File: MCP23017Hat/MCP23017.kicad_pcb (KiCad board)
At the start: 2 copper layers, 65 x 56 mm, 12 parts, among them J0 RPi_GPIO, J1 Address Jumper, T1 GP0, T2 GP1, U1 MCP23017

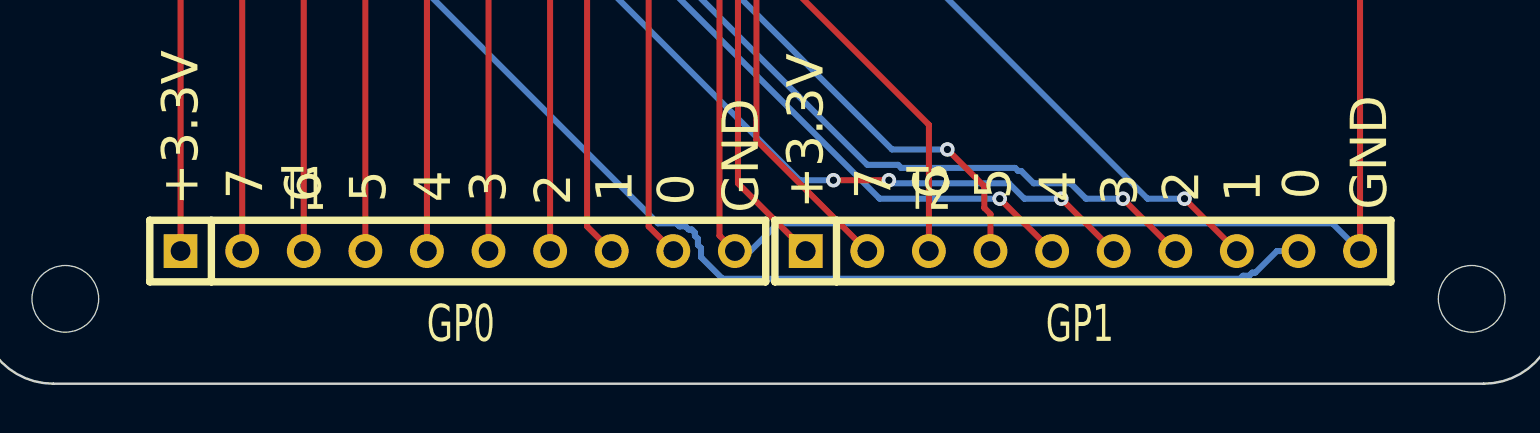
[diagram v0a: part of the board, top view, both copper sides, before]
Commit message: Update screw terminals on all HATs.
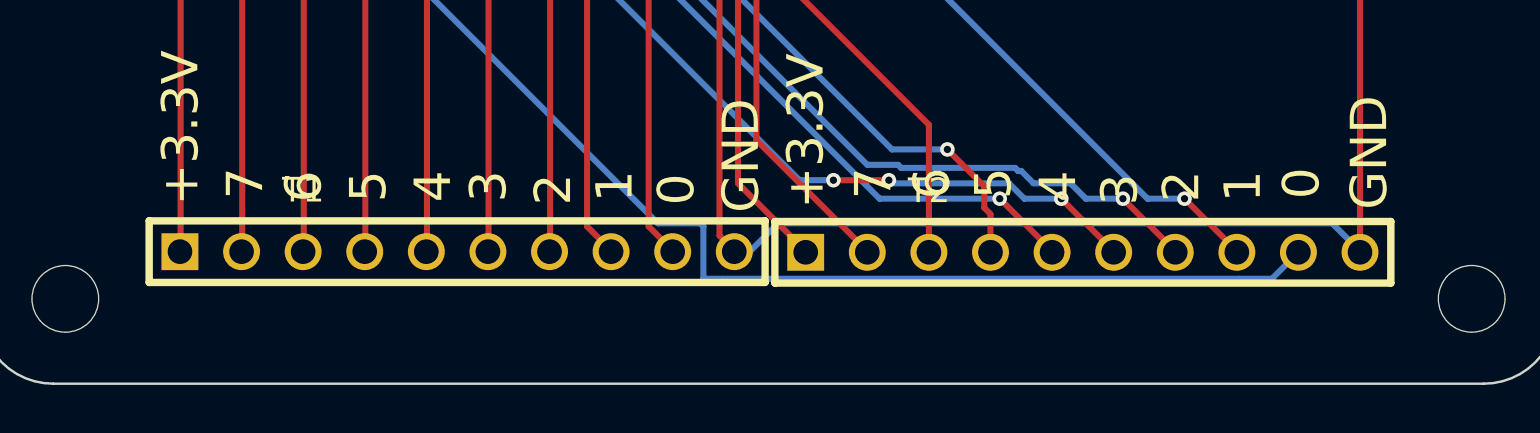
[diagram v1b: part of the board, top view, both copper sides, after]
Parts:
- T1, T2: footprint SIL-10 -> ScrewTerm_2.54-10
- moved T1 6.38 mm to (51.4, 82.4)
- moved T2 6.35 mm to (77.2, 82.5)
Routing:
- net N-000009: track 52.3 -> 53.1 mm

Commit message: Minor updates
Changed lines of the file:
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@@
   )
   (module ScrewTerm_2.54-10 (layer F.Cu)
-    (at 77.216 82.4738)
+    (at 77.216 82.4484)
     (descr "Screw Terminals, 2.54 pitch, 10 position")
     (tags CONN)

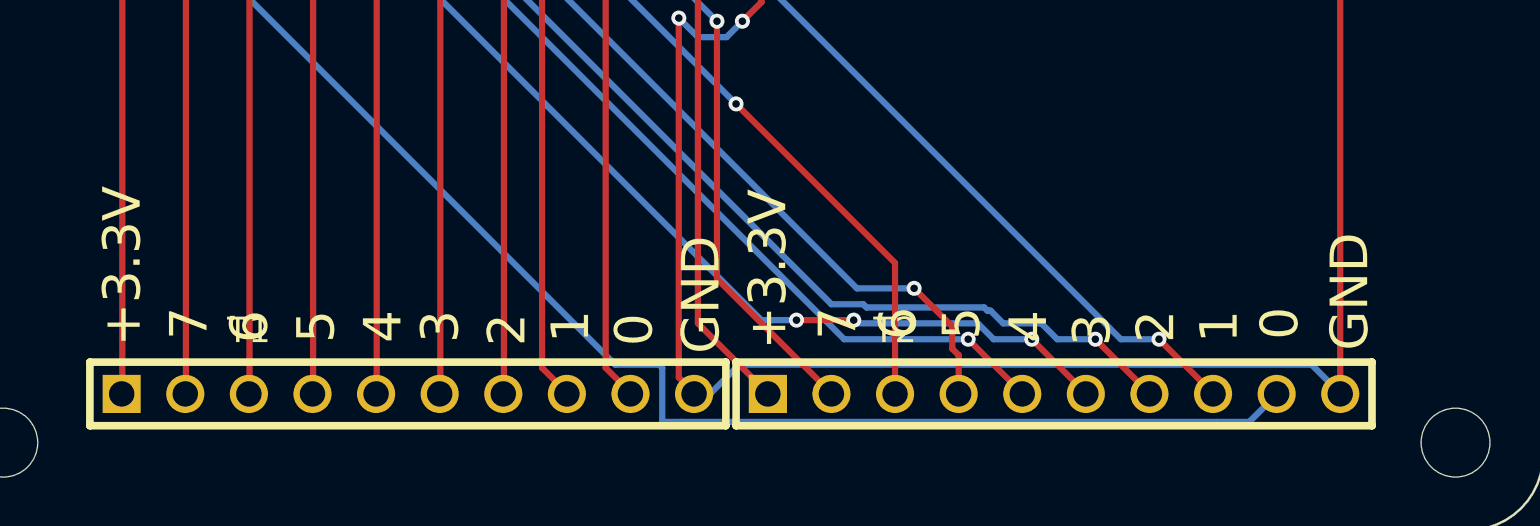
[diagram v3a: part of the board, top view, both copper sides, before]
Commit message: Move terminal markings to be more visible once the terminal blocks have been installed.
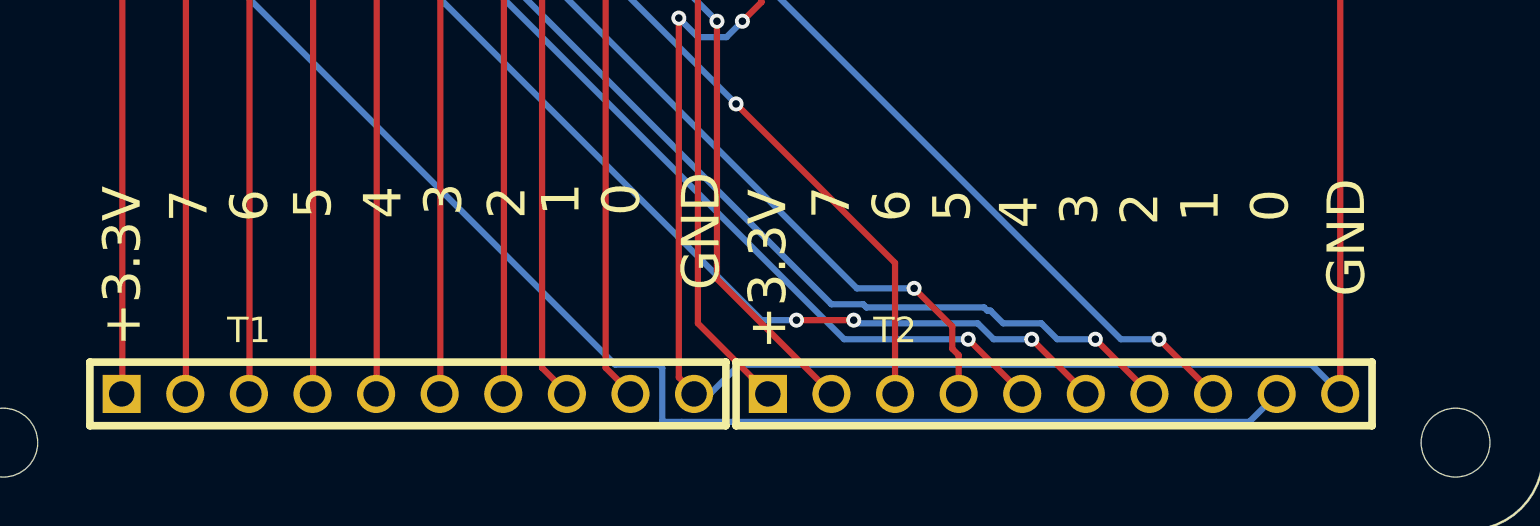
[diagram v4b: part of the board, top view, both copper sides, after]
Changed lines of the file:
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@@
       (effects (font (size 1.016 1.016) (thickness 0.2032)))
     )
-    (fp_text value GP1 (at 0 2.54) (layer F.SilkS) hide
+    (fp_text value GP1 (at 21.336 -2.1844) (layer F.SilkS) hide
       (effects (font (size 1.016 1.016) (thickness 0.2032)))
     )
@@
       (effects (font (size 1.016 1.016) (thickness 0.2032)))
     )
-    (fp_text value GP0 (at 0 2.54) (layer F.SilkS) hide
+    (fp_text value GP0 (at -8.8646 -2.3114) (layer F.SilkS) hide
       (effects (font (size 1.016 1.016) (thickness 0.2032)))
     )
@@
     (effects (font (size 1.5 1.5) (thickness 0.3)))
   )
-  (gr_text 7 (at 49.022 79.629 90) (layer F.SilkS)
-    (effects (font (size 1.5 1.5) (thickness 0.3)))
-  )
-  (gr_text 6 (at 51.435 79.756 90) (layer F.SilkS)
-    (effects (font (size 1.5 1.5) (thickness 0.3)))
-  )
-  (gr_text 5 (at 54.102 79.756 90) (layer F.SilkS)
-    (effects (font (size 1.5 1.5) (thickness 0.3)))
-  )
-  (gr_text 4 (at 56.769 79.756 90) (layer F.SilkS)
-    (effects (font (size 1.5 1.5) (thickness 0.3)))
-  )
-  (gr_text 3 (at 59.055 79.756 90) (layer F.SilkS)
-    (effects (font (size 1.5 1.5) (thickness 0.3)))
-  )
-  (gr_text 2 (at 61.722 79.883 90) (layer F.SilkS)
-    (effects (font (size 1.5 1.5) (thickness 0.3)))
-  )
-  (gr_text 1 (at 64.262 79.756 90) (layer F.SilkS)
-    (effects (font (size 1.5 1.5) (thickness 0.3)))
-  )
-  (gr_text 0 (at 66.802 79.883 90) (layer F.SilkS)
-    (effects (font (size 1.5 1.5) (thickness 0.3)))
-  )
-  (gr_text GND (at 69.469 78.486 90) (layer F.SilkS)
-    (effects (font (size 1.5 1.5) (thickness 0.3)))
-  )
-  (gr_text GND (at 95.377 78.359 90) (layer F.SilkS)
-    (effects (font (size 1.5 1.5) (thickness 0.3)))
-  )
-  (gr_text 0 (at 92.583 79.629 90) (layer F.SilkS)
-    (effects (font (size 1.5 1.5) (thickness 0.3)))
-  )
-  (gr_text 1 (at 90.17 79.756 90) (layer F.SilkS)
-    (effects (font (size 1.5 1.5) (thickness 0.3)))
-  )
-  (gr_text 2 (at 87.63 79.756 90) (layer F.SilkS)
-    (effects (font (size 1.5 1.5) (thickness 0.3)))
-  )
-  (gr_text 3 (at 85.09 79.883 90) (layer F.SilkS)
-    (effects (font (size 1.5 1.5) (thickness 0.3)))
-  )
-  (gr_text 4 (at 82.55 79.756 90) (layer F.SilkS)
-    (effects (font (size 1.5 1.5) (thickness 0.3)))
-  )
-  (gr_text 5 (at 79.883 79.629 90) (layer F.SilkS)
-    (effects (font (size 1.5 1.5) (thickness 0.3)))
-  )
-  (gr_text 6 (at 77.343 79.629 90) (layer F.SilkS)
-    (effects (font (size 1.5 1.5) (thickness 0.3)))
-  )
-  (gr_text 7 (at 74.93 79.629 90) (layer F.SilkS)
-    (effects (font (size 1.5 1.5) (thickness 0.3)))
-  )
+  (gr_text 7 (at 49.022 74.93 90) (layer F.SilkS)
+    (effects (font (size 1.5 1.5) (thickness 0.3)))
+  )
+  (gr_text 6 (at 51.435 74.93 90) (layer F.SilkS)
+    (effects (font (size 1.5 1.5) (thickness 0.3)))
+  )
+  (gr_text 5 (at 53.975 74.803 90) (layer F.SilkS)
+    (effects (font (size 1.5 1.5) (thickness 0.3)))
+  )
+  (gr_text 4 (at 56.769 74.803 90) (layer F.SilkS)
+    (effects (font (size 1.5 1.5) (thickness 0.3)))
+  )
+  (gr_text 3 (at 59.182 74.676 90) (layer F.SilkS)
+    (effects (font (size 1.5 1.5) (thickness 0.3)))
+  )
+  (gr_text 2 (at 61.722 74.803 90) (layer F.SilkS)
+    (effects (font (size 1.5 1.5) (thickness 0.3)))
+  )
+  (gr_text 1 (at 63.881 74.676 90) (layer F.SilkS)
+    (effects (font (size 1.5 1.5) (thickness 0.3)))
+  )
+  (gr_text 0 (at 66.294 74.676 90) (layer F.SilkS)
+    (effects (font (size 1.5 1.5) (thickness 0.3)))
+  )
+  (gr_text GND (at 69.469 75.946 90) (layer F.SilkS)
+    (effects (font (size 1.5 1.5) (thickness 0.3)))
+  )
+  (gr_text GND (at 95.25 76.2 90) (layer F.SilkS)
+    (effects (font (size 1.5 1.5) (thickness 0.3)))
+  )
+  (gr_text 0 (at 92.202 74.93 90) (layer F.SilkS)
+    (effects (font (size 1.5 1.5) (thickness 0.3)))
+  )
+  (gr_text 1 (at 89.408 74.93 90) (layer F.SilkS)
+    (effects (font (size 1.5 1.5) (thickness 0.3)))
+  )
+  (gr_text 2 (at 86.995 75.057 90) (layer F.SilkS)
+    (effects (font (size 1.5 1.5) (thickness 0.3)))
+  )
+  (gr_text 3 (at 84.582 75.057 90) (layer F.SilkS)
+    (effects (font (size 1.5 1.5) (thickness 0.3)))
+  )
+  (gr_text 4 (at 82.169 75.184 90) (layer F.SilkS)
+    (effects (font (size 1.5 1.5) (thickness 0.3)))
+  )
+  (gr_text 5 (at 79.502 74.93 90) (layer F.SilkS)
+    (effects (font (size 1.5 1.5) (thickness 0.3)))
+  )
+  (gr_text 6 (at 77.089 74.93 90) (layer F.SilkS)
+    (effects (font (size 1.5 1.5) (thickness 0.3)))
+  )
+  (gr_text 7 (at 74.676 74.803 90) (layer F.SilkS)
+    (effects (font (size 1.5 1.5) (thickness 0.3)))
+  )
